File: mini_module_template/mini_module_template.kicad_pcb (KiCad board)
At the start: 4 copper layers, 100 x 60 mm, 158 parts, among them IC1 TJA1044GTK_3Z, J1 SWD, J4 USB_C_Receptacle_USB2.0, Q1 S9013, Q2 AO3400A, SW2 NRST, SW4 SW_DIP_x01, U1 STM32F303CBTx, U2 FM24CL16B, U3 STM32F103CB, U4 AZ1117-3.3, U5 TPS563200, U6 IP4220CZ6, U7 SL2.1A, U8 TS3USB30EDGSR, Y1 8MHz, Y2 8MHz, Y4 12Mhz

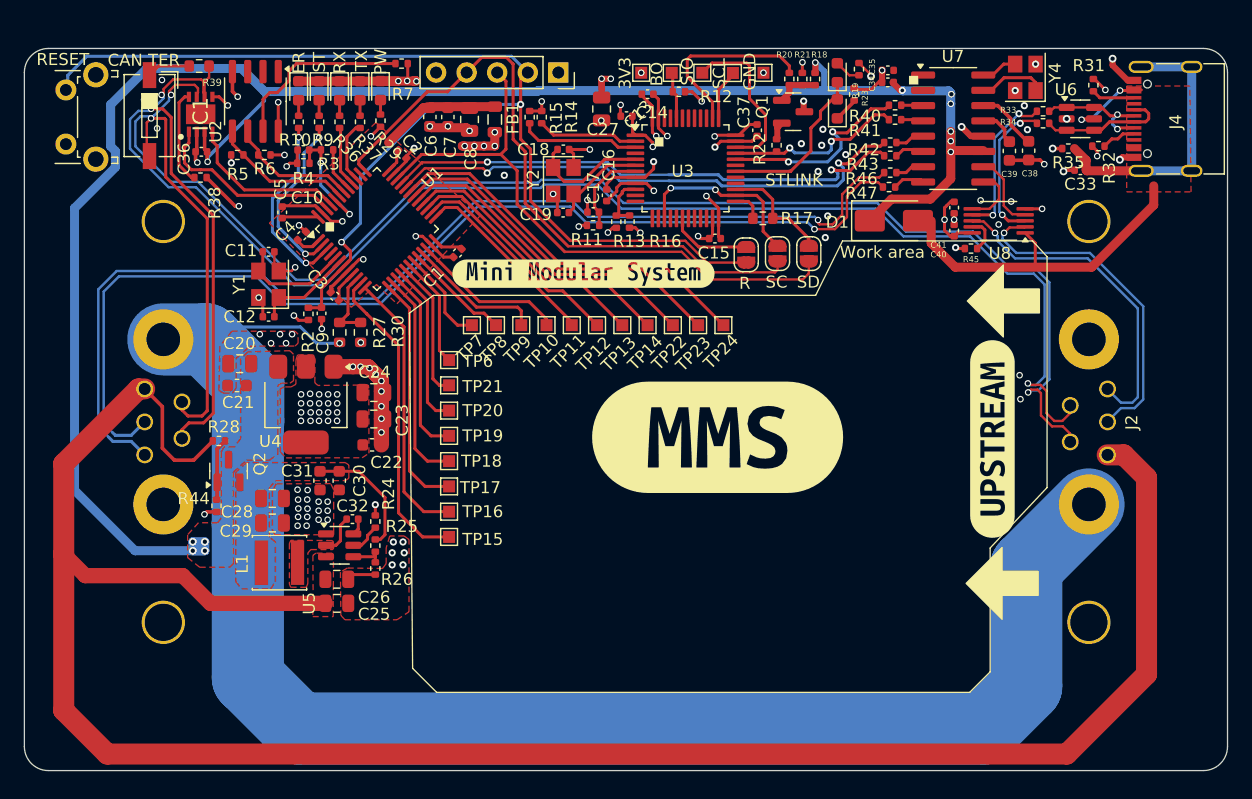
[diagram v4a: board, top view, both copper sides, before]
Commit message: revison C, aded 2 can support and gight voltage input stepdown
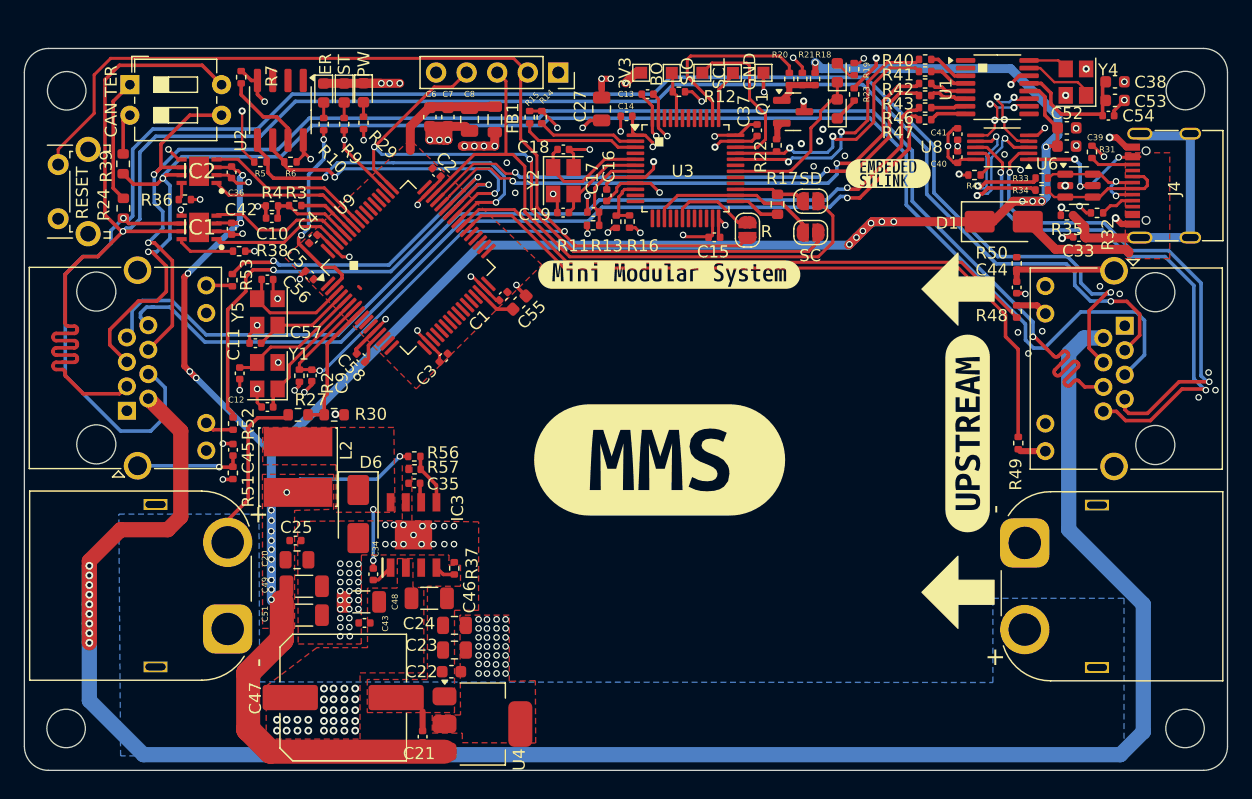
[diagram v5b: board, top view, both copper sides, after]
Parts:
- removed C26: 10u, Capacitor_SMD:C_0805_2012Metric
- removed C28, C29: 22u, Capacitor_SMD:C_0805_2012Metric
- removed C30: 100n, Capacitor_SMD:C_0603_1608Metric
- removed C31: 1n, Capacitor_SMD:C_0603_1608Metric
- removed C32: 100n, Capacitor_SMD:C_0402_1005Metric
- removed D8: LED_RXD, Diode_SMD:D_0603_1608Metric
- removed D9: LED_TXD, Diode_SMD:D_0603_1608Metric
- removed J3: ~, parts:DSUB-7w2
- removed L1: 3.3u, Inductor_SMD:L_Changjiang_FNR4030S
- removed Q2: AO3400A, Package_TO_SOT_SMD:SOT-23
- removed R25: 54k9, Resistor_SMD:R_0402_1005Metric
- removed R26: 10k, Resistor_SMD:R_0402_1005Metric
- removed R28: 1k, Resistor_SMD:R_0402_1005Metric
- removed R44: 100k, Resistor_SMD:R_0402_1005Metric
- removed SW4: SW_DIP_x01, Button_Switch_SMD:SW_DIP_SPSTx01_Slide_6.7x4.1mm_W6.73mm_P2.54mm_LowProfile_JPin
- removed TP10, TP11, TP12, TP13, TP14, TP15, TP16, TP17, TP18, TP19, TP20, TP21, TP22, TP23, TP24, TP6, TP7, TP8, TP9: TestPoint, TestPoint:TestPoint_Pad_1.0x1.0mm
- removed U5: TPS563200, Package_TO_SOT_SMD:SOT-23-6
- removed U7: SL2.1A, Package_SO:SOP-16_3.9x9.9mm_P1.27mm
- removed kibuzzard-673144D2: G***, kibuzzard-673144D2
- removed kibuzzard-673144DF: G***, kibuzzard-673144DF
- removed kibuzzard-673144EC: G***, kibuzzard-673144EC
- removed kibuzzard-6731459B: G***, kibuzzard-6731459B
- removed kibuzzard-673145AA: G***, kibuzzard-673145AA
- removed kibuzzard-6731503D: G***, kibuzzard-6731503D
- removed kibuzzard-67315047: G***, kibuzzard-67315047
- removed kibuzzard-673150A6: G***, kibuzzard-673150A6
- removed kibuzzard-673150B2: G***, kibuzzard-673150B2
- removed kibuzzard-673150BD: G***, kibuzzard-673150BD
- added C42: 100n, Capacitor_SMD:C_0402_1005Metric, F.Cu at (97.2, 75.0)
- added C43: 100n, Capacitor_SMD:C_0402_1005Metric, F.Cu at (108.3, 107.8)
- added C44: 10n, Capacitor_SMD:C_0402_1005Metric, F.Cu at (162.5, 79.9)
- added C45: 10n, Capacitor_SMD:C_0402_1005Metric, F.Cu at (97.3, 93.4)
- added C46: 2.2u, Capacitor_SMD:C_1206_3216Metric, F.Cu at (113.6, 105.7)
- added C47: 47u, Capacitor_SMD:C_Elec_10x10.2, F.Cu at (106.5, 114.0)
- added C48: 2.2u, Capacitor_SMD:C_1206_3216Metric, F.Cu at (108.0, 106.0)
- added C49: 47u, Capacitor_SMD:C_1206_3216Metric, F.Cu at (103.3, 104.7)
- added C51: 47u, Capacitor_SMD:C_1206_3216Metric, F.Cu at (103.3, 107.1)
- added C52: 100n, Capacitor_SMD:C_0603_1608Metric, F.Cu at (166.7, 66.6)
- added C53: 1u, Capacitor_SMD:C_0603_1608Metric, F.Cu at (170.7, 64.3)
- added C54: 100n, Capacitor_SMD:C_0402_1005Metric, F.Cu at (170.1, 65.6)
- added C55: 2.2u, Capacitor_SMD:C_0603_1608Metric, F.Cu at (121.2, 81.1)
- added C56: 6P, Capacitor_SMD:C_0402_1005Metric, F.Cu at (100.2, 79.2)
- added C57: 6P, Capacitor_SMD:C_0402_1005Metric, F.Cu at (99.2, 84.5)
- added C58: 100n, Capacitor_SMD:C_0402_1005Metric, F.Cu at (108.0, 85.7)
- added D6: SS34, Diode_SMD:D_SMA, F.Cu at (107.8, 98.7)
- added H1: ~, MountingHole:MountingHole_3.2mm_M3, F.Cu at (176.5, 116.5)
- added H2: ~, MountingHole:MountingHole_3.2mm_M3, F.Cu at (83.5, 116.5)
- added H3: ~, MountingHole:MountingHole_3.2mm_M3, F.Cu at (176.5, 63.5)
- added H4: ~, MountingHole:MountingHole_3.2mm_M3, F.Cu at (83.5, 63.5)
- added IC2: TJA1044GTK_3Z, parts:SON65P300X300X100-9N-D, F.Cu at (94.5, 70.2)
- added IC3: LMR16030SDDAR, parts:SOIC127P600X170-9N, F.Cu at (112.3, 100.4)
- added J6: Conn_01x02, Connector_AMASS:AMASS_XT60PW-M_1x02_P7.20mm_Horizontal, F.Cu at (96.9, 108.2)
- added J7: RJ45_LED_Shielded, Connector_RJ:RJ45_Amphenol_RJHSE538X, F.Cu at (171.5, 83.0)
- added J8: RJ45_LED_Shielded, Connector_RJ:RJ45_Amphenol_RJHSE538X, F.Cu at (88.5, 90.1)
- added L2: 8.2u, Inductor_SMD:L_Cenker_CKCS6045, F.Cu at (102.8, 94.8)
- added R48: 1k, Resistor_SMD:R_0402_1005Metric, F.Cu at (162.5, 81.9)
- added R49: 1k, Resistor_SMD:R_0402_1005Metric, F.Cu at (162.6, 92.8)
- added R50: 33k, Resistor_SMD:R_0402_1005Metric, F.Cu at (162.5, 77.9)
- added R51: 33k, Resistor_SMD:R_0402_1005Metric, F.Cu at (97.3, 95.3)
- added R52: 1k, Resistor_SMD:R_0402_1005Metric, F.Cu at (97.3, 91.2)
- added R53: 1k, Resistor_SMD:R_0402_1005Metric, F.Cu at (97.3, 79.3)
- added R56: 100k, Resistor_SMD:R_0402_1005Metric, F.Cu at (112.4, 93.9)
- added R57: 17,8k, Resistor_SMD:R_0402_1005Metric, F.Cu at (112.4, 95.0)
- added SW5: SW_DIP_x02, Button_Switch_THT:SW_DIP_SPSTx02_Slide_6.7x6.64mm_W7.62mm_P2.54mm_LowProfile, F.Cu at (88.8, 63.0)
- added U9: STM32F446RETx, Package_QFP:LQFP-64_10x10mm_P0.5mm, F.Cu at (111.9, 78.2)
- added Y5: 32.768KHz, Crystal:Crystal_SMD_3225-4Pin_3.2x2.5mm, F.Cu at (100.2, 81.9)
- added kibuzzard-674CE2D2: G***, kibuzzard-674CE2D2, F.Cu at (151.8, 70.4)
- C21: footprint Capacitor_SMD:C_0603_1608Metric -> Capacitor_SMD:C_0402_1005Metric
- C25: value 10u -> 100n; footprint Capacitor_SMD:C_0805_2012Metric -> Capacitor_SMD:C_0402_1005Metric
- C35: value 1n -> 100n
- D1: value D_Schottky -> ss34
- J2: value ~ -> Conn_01x02; footprint parts:DSUB-7w2 -> Connector_AMASS:AMASS_XT60PW-M_1x02_P7.20mm_Horizontal
- R24: value 10k -> 120R; footprint Resistor_SMD:R_0402_1005Metric -> Resistor_SMD:R_0603_1608Metric
- R36: value 1k -> 10k
- R37: value 1k -> 49,9k
- U1: value STM32F303CBTx -> CH334R; footprint Package_QFP:LQFP-48_7x7mm_P0.5mm -> Package_SO:QSOP-16_3.9x4.9mm_P0.635mm
- moved C34 59.2 mm to (109.0, 103.7), turned to 90 degrees
- moved U1 52.9 mm to (160.9, 63.2), turned to 0 degrees
- moved C35 52.2 mm to (112.4, 96.1), turned to 0 degrees
- moved R37 37.9 mm to (115.7, 103.2)
- moved R24 33.4 mm to (88.2, 73.3)
- moved C21 33.0 mm to (113.1, 117.2), turned to 90 degrees
- moved U4 30.3 mm to (118.1, 116.2), turned to 0 degrees
- moved C24 20.5 mm to (115.8, 108.0), turned to 180 degrees
- moved C23 20.3 mm to (115.8, 110.0), turned to 180 degrees
- moved C22 20.0 mm to (115.5, 111.8), turned to 180 degrees
- moved C20 17.0 mm to (102.7, 102.5), turned to 0 degrees
- moved R36 14.4 mm to (93.3, 72.6), turned to 180 degrees
- moved R7 13.4 mm to (98.0, 62.4), turned to -90 degrees
- moved J2 11.4 mm to (163.2, 101.1), turned to -90 degrees
- moved C3 10.4 mm to (114.8, 85.7), turned to -135 degrees
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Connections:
- C11 pad 2: Net-(U1-PF0) -> Net-(U9-PH0)
- C12 pad 2: Net-(U1-PF1) -> Net-(U9-PH1)
- C25 pad 1: +12V -> +5V
- C34 pad 1: +5V -> Net-(IC3-BOOT)
- C34 pad 2: GND -> /POWER/5V_COIL
- C35 pad 1: +5V -> GND
- C35 pad 2: GND -> Net-(IC3-SS)
- C38 pad 2: Net-(U7-VDD18) -> Net-(U1-VDD33)
- C39 pad 2: Net-(U7-VDD33) -> +5V
- IC1 pad 1: /CAN/CAN_TXD -> /CAN/CAN1_TXD
- IC1 pad 4: /CAN/CAN_RXD -> /CAN/CAN1_RXD
- IC1 pad 6: /CAN/CAN- -> /CAN/CAN1-
- IC1 pad 7: /CAN/CAN+ -> /CAN/CAN1+
- J2 pad 1: VCC -> GND
- J2 pad 2: +12V -> VCC
- R24 pad 1: Net-(U5-EN) -> /CAN/CAN1-
- R24 pad 2: GND -> Net-(R24-Pad2)
- R36 pad 1: /CAN/RXD_LED -> GND
- R37 pad 1: /CAN/TXD_LED -> Net-(IC3-RT/SYNC)
- R37 pad 2: Net-(D9-A) -> GND
- R39 pad 1: /CAN/CAN- -> /CAN/CAN2+
- R40 pad 1: Net-(U7-DM3) -> Net-(U1-DM3)
- R41 pad 2: Net-(U7-DP3) -> Net-(U1-DP3)
- R42 pad 2: Net-(U7-DM2) -> Net-(U1-DM2)
- R43 pad 2: Net-(U7-DP2) -> Net-(U1-DP2)
- R46 pad 1: Net-(U7-DM1) -> Net-(U1-DM1)
- R46 pad 2: /POWER/USB_DOWNSTREAM_D- -> /CAN/USB_DOWNSTREAM_D-
- R47 pad 1: /POWER/USB_DOWNSTREAM_D+ -> /CAN/USB_DOWNSTREAM_D+
- R47 pad 2: Net-(U7-DP1) -> Net-(U1-DP1)
- R5 pad 2: /MCU/SDA -> /MCU/I2C3_SDA
- R6 pad 2: /MCU/SCL -> /MCU/I2C3_SCL
- U1 pad 1: /MCU/3V3_MCU -> unconnected-(U1-DM4-Pad1)
- U1 pad 10: /MCU/V_SENSE -> /USB/USB_UPSTREAM_D-
- U1 pad 11: PA1 -> /USB/USB_UPSTREAM_D+
- U1 pad 12: PA2 -> +5V
- U1 pad 13: PA3 -> Net-(U1-VDD33)
- U1 pad 14: PA4 -> GND
- U1 pad 15: PA5 -> Net-(U1-XO)
- U1 pad 16: PA6 -> Net-(U1-XI)
- U1 pad 2: /MCU/USR_LED1 -> unconnected-(U1-DP4-Pad2)
- U1 pad 3: /MCU/USR_LED2 -> Net-(U1-DM3)
- U1 pad 4: /MCU/USR_BTN -> Net-(U1-DP3)
- U1 pad 5: Net-(U1-PF0) -> Net-(U1-DM2)
- U1 pad 6: Net-(U1-PF1) -> Net-(U1-DP2)
- U1 pad 7: /MCU/NRST -> Net-(U1-DM1)
- U1 pad 8: GND -> Net-(U1-DP1)
- U1 pad 9: /MCU/3V3_MCU -> unconnected-(U1-RESET#/CDP-Pad9)
- U2 pad 5: /MCU/SDA -> /MCU/I2C3_SDA
- U2 pad 6: /MCU/SCL -> /MCU/I2C3_SCL
- U8 pad 2: /POWER/USB_UPSTREAM_D+ -> /CAN/USB_UPSTREAM_D+
- U8 pad 8: /POWER/USB_UPSTREAM_D- -> /CAN/USB_UPSTREAM_D-
- Y1 pad 1: Net-(U1-PF1) -> Net-(U9-PH1)
- Y1 pad 3: Net-(U1-PF0) -> Net-(U9-PH0)
- Y4 pad 1: Net-(U7-XOUT) -> Net-(U1-XO)
- Y4 pad 3: Net-(U7-XIN) -> Net-(U1-XI)
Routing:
- net /CAN/CAN1+: track 0.00 -> 167.2 mm, vias 0 -> 2
- net /CAN/CAN-: track 150.7 -> 0.00 mm, vias 3 -> 0
- net /CAN/CAN+: track 148.2 -> 0.00 mm, vias 3 -> 0
- net /CAN/CAN1-: track 0.00 -> 144.5 mm, vias 0 -> 2
- net /CAN/CAN2-: track 0.00 -> 128.5 mm, vias 0 -> 3
- net /CAN/CAN2+: track 0.00 -> 128.1 mm, vias 0 -> 2
- net VCC: track 135.6 -> 14.5 mm, vias 1 -> 28
- net /POWER/USB_DOWNSTREAM_D-: track 90.4 -> 0.00 mm, vias 1 -> 0
- net /POWER/USB_DOWNSTREAM_D+: track 89.0 -> 0.00 mm, vias 1 -> 0
- net /CAN/USB_DOWNSTREAM_D-: track 0.00 -> 78.6 mm, vias 0 -> 1
- net /CAN/USB_DOWNSTREAM_D+: track 0.00 -> 77.0 mm, vias 0 -> 1
- net /CAN/TXD1_LED: track 0.00 -> 59.2 mm
- net /CAN/RXD1_LED: track 0.00 -> 50.3 mm
- net +5V: track 156.8 -> 203.1 mm, vias 12 -> 28
- net /CAN/USB_UPSTREAM_D-: track 0.00 -> 44.3 mm, vias 0 -> 2
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- added copper zone on B.Cu, net VCC
- added copper zone on F.Cu, net VCC
- removed copper zone on F.Cu, net +12V
- removed copper zone on F.Cu, net /POWER/5V_mosfet
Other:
- board text added: "12V"
- board text added: "C1+"
- board text added: "C1-"
- board text added: "C2+"
- board text added: "C2-"
- board text added: "D+"
- board text added: "D-"
- board text removed: "RX"
- board text removed: "STLINK"
- board text removed: "TX"
- board text removed: "Work area"
